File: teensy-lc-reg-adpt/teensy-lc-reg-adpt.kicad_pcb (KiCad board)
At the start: 2 copper layers, 10.2 x 27.9 mm, 7 parts

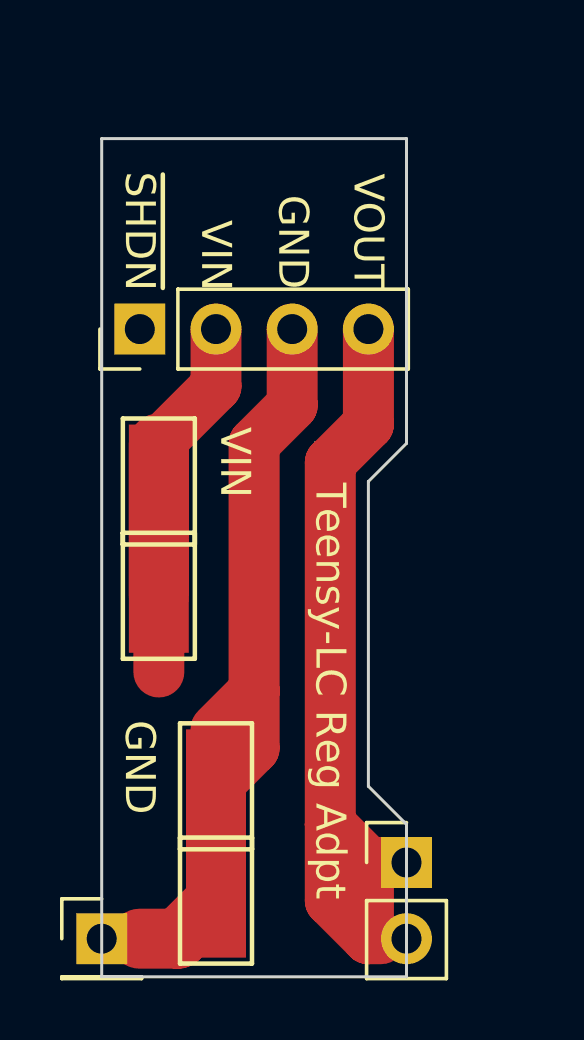
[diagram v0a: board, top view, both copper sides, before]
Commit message: update teensy-lc-reg-adpt R2 with Vin monitor
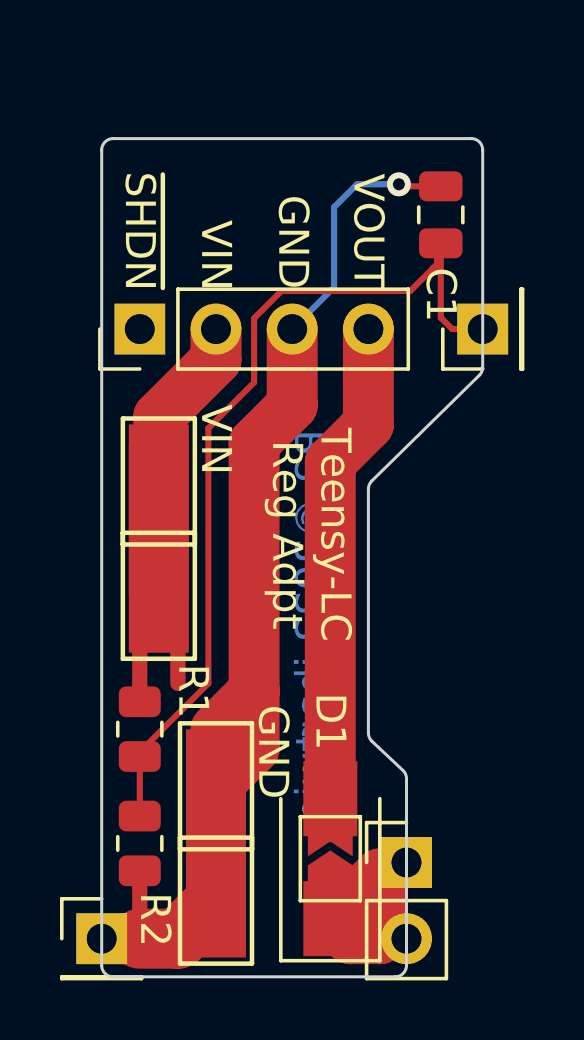
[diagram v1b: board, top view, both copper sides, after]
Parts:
- added C1: C_Small, Capacitor_SMD:C_0805_2012Metric, F.Cu at (159.9, 85.1)
- added D1: SK220, Diode_SMD:D_SMA, F.Cu at (156.2, 106.6)
- added J4: Conn_01x01, Connector_PinHeader_2.54mm:PinHeader_1x01_P2.54mm_Vertical, F.Cu at (161.3, 88.9)
- added JP1: SolderJumper_2_Open, Jumper:SolderJumper-2_P1.3mm_Open_TrianglePad1.0x1.5mm, F.Cu at (156.2, 106.6)
- added R1: R_Small, Resistor_SMD:R_0805_2012Metric, F.Cu at (149.9, 102.2)
- added R2: R_Small, Resistor_SMD:R_0805_2012Metric, F.Cu at (149.9, 106.0)
- J1: renamed from REF**; value PinHeader_1x01_P2.54mm_Vertical -> Conn_01x01
- J2: renamed from REF**; value PinHeader_1x04_P2.54mm_Vertical -> Conn_01x04
- J3: renamed from REF**; value PinHeader_1x02_P2.54mm_Vertical -> Conn_01x02
- TP1, TP2, TP3, TP4: renamed from REF**; value TestPoint_Keystone_5019_Minature -> TestPoint
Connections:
- J1 pad 1: (no net) -> GND
- J2 pad 1: (no net) -> unconnected-(J2-Pad1)
- J2 pad 2: (no net) -> +12V
- J2 pad 3: (no net) -> GND
- J2 pad 4: (no net) -> +5V
- J3 pad 1: (no net) -> /VBUS
- J3 pad 2: (no net) -> /VBUS
- TP1 pad 1: (no net) -> +12V
- TP2 pad 1: (no net) -> GND
- TP3 pad 1: (no net) -> +12V
- TP4 pad 1: (no net) -> GND
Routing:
- net (no net): track 63.7 -> 0.00 mm
- net GND: track 0.00 -> 35.6 mm, vias 0 -> 1
- net /P12V_SENSE: track 0.00 -> 30.1 mm
- net +12V: track 0.00 -> 18.2 mm
- net +5V: track 0.00 -> 16.2 mm
- net /VBUS: track 0.00 -> 6.35 mm
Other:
- board size 10.2 x 27.9 mm -> 12.7 x 27.9 mm
- board text added: "R2 ©2022 ihartwig"
- board text added: "VSENSE"
- board text removed: "R1 ©2022 ihartwig"
